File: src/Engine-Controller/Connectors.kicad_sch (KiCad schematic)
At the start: 9 parts, among them P3 SBH11-PBPC-D10-RA-BK, P4 0901471110, P5 66953-005LF, P7 0901471110, U4 SN74LV07ADR

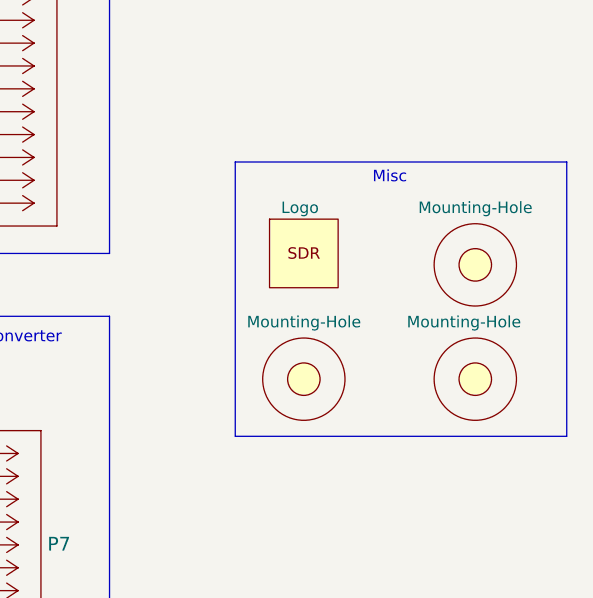
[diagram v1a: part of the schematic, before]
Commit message: Removed misc elements from connectors sheet
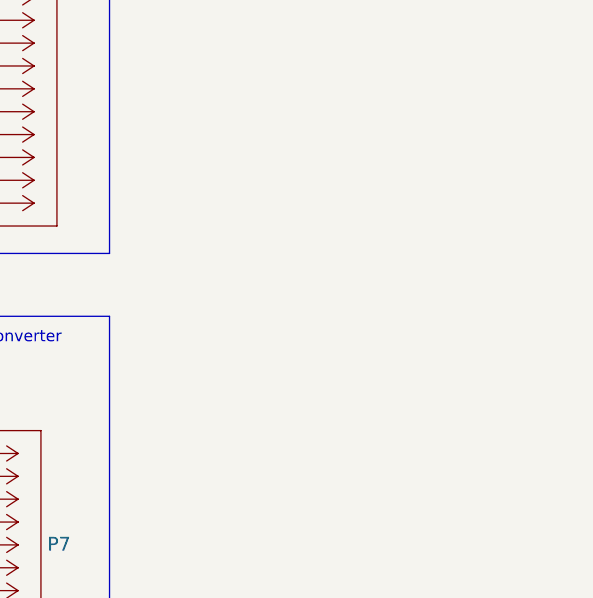
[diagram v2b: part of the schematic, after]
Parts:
- removed H1, H2, H3: Mounting-Hole, Engine-Controller:MountingHole_4.3mm_M4_DIN965, symbol Engine-Controller:Mounting-Hole
- removed LOGO1: Logo, Engine-Controller:Logo, symbol Engine-Controller:Logo
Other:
- note removed: "Misc"
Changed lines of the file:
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@@
-    (stroke (width 0) (type default) (color 0 0 0 0))
-  )
-  (polyline (pts (xy 273.05 68.58) (xy 273.05 99.06))
     (stroke (width 0) (type default) (color 0 0 0 0))
   )
@@
     (stroke (width 0) (type default) (color 0 0 0 0))
   )
-  (polyline (pts (xy 236.22 99.06) (xy 236.22 68.58))
-    (stroke (width 0) (type default) (color 0 0 0 0))
-  )
   (wire (pts (xy 143.51 108.585) (xy 143.51 113.665))
     (stroke (width 0) (type default) (color 0 0 0 0))
@@
     (stroke (width 0) (type default) (color 0 0 0 0))
   )
-  (polyline (pts (xy 273.05 99.06) (xy 236.22 99.06))
-    (stroke (width 0) (type default) (color 0 0 0 0))
-  )
   (wire (pts (xy 143.51 118.745) (xy 143.51 123.825))
     (stroke (width 0) (type default) (color 0 0 0 0))
@@
   )
   (wire (pts (xy 192.278 73.152) (xy 203.708 73.152))
-    (stroke (width 0) (type default) (color 0 0 0 0))
-  )
-  (polyline (pts (xy 236.22 68.58) (xy 273.05 68.58))
     (stroke (width 0) (type default) (color 0 0 0 0))
   )
@@
   )
   (text "Serial Connector" (at 142.24 43.815 0)
-    (effects (font (size 1.27 1.27)) (justify left bottom))
-  )
-  (text "Misc" (at 251.46 71.12 0)
     (effects (font (size 1.27 1.27)) (justify left bottom))
   )
@@
     (pin "9")
   )
-  (symbol (lib_id "Engine-Controller:Logo") (at 243.84 78.74 0) (unit 1)
-    (in_bom yes) (on_board yes)
-    (property "Reference" "LOGO1" (id 0) (at 248.3612 77.5716 0)
-      (effects (font (size 1.27 1.27)) (justify left) hide)
-    )
-    (property "Value" "Logo" (id 1) (at 241.3 73.66 0)
-      (effects (font (size 1.27 1.27)) (justify left))
-    )
-    (property "Footprint" "Engine-Controller:Logo" (id 2) (at 243.84 78.74 0)
-      (effects (font (size 1.27 1.27)) hide)
-    )
-    (property "Datasheet" "" (id 3) (at 243.84 78.74 0)
-      (effects (font (size 1.27 1.27)) hide)
-    )
-  )
-  (symbol (lib_id "Engine-Controller:Mounting-Hole") (at 243.84 92.71 0) (unit 1)
-    (in_bom yes) (on_board yes)
-    (property "Reference" "H1" (id 0) (at 249.1232 91.5416 0)
-      (effects (font (size 1.27 1.27)) (justify left) hide)
-    )
-    (property "Value" "Mounting-Hole" (id 1) (at 237.49 86.36 0)
-      (effects (font (size 1.27 1.27)) (justify left))
-    )
-    (property "Footprint" "Engine-Controller:MountingHole_4.3mm_M4_DIN965" (id 2) (at 243.84 92.71 0)
-      (effects (font (size 1.27 1.27)) hide)
-    )
-    (property "Datasheet" "" (id 3) (at 243.84 92.71 0)
-      (effects (font (size 1.27 1.27)) hide)
-    )
-  )
-  (symbol (lib_id "Engine-Controller:Mounting-Hole") (at 262.89 80.01 0) (unit 1)
-    (in_bom yes) (on_board yes)
-    (property "Reference" "H2" (id 0) (at 268.1732 78.8416 0)
-      (effects (font (size 1.27 1.27)) (justify left) hide)
-    )
-    (property "Value" "Mounting-Hole" (id 1) (at 256.54 73.66 0)
-      (effects (font (size 1.27 1.27)) (justify left))
-    )
-    (property "Footprint" "Engine-Controller:MountingHole_4.3mm_M4_DIN965" (id 2) (at 262.89 80.01 0)
-      (effects (font (size 1.27 1.27)) hide)
-    )
-    (property "Datasheet" "" (id 3) (at 262.89 80.01 0)
-      (effects (font (size 1.27 1.27)) hide)
-    )
-  )
-  (symbol (lib_id "Engine-Controller:Mounting-Hole") (at 262.89 92.71 0) (unit 1)
-    (in_bom yes) (on_board yes)
-    (property "Reference" "H3" (id 0) (at 268.1732 91.5416 0)
-      (effects (font (size 1.27 1.27)) (justify left) hide)
-    )
-    (property "Value" "Mounting-Hole" (id 1) (at 255.27 86.36 0)
-      (effects (font (size 1.27 1.27)) (justify left))
-    )
-    (property "Footprint" "Engine-Controller:MountingHole_4.3mm_M4_DIN965" (id 2) (at 262.89 92.71 0)
-      (effects (font (size 1.27 1.27)) hide)
-    )
-    (property "Datasheet" "" (id 3) (at 262.89 92.71 0)
-      (effects (font (size 1.27 1.27)) hide)
-    )
-  )
   (symbol (lib_id "Engine-Controller:SN74LV07ADR") (at 77.724 49.276 0) (unit 1)
